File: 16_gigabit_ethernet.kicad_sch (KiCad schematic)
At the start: 29 parts, among them J500 JXD1-1022NL recessed 1GbE RJ45, U500 RTL8111H-CG-RH PCIe Gigabit E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, U501 D3V3XA4B10LP-7 four-channel 0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, U502 D3V3XA4B10LP-7 four-channel 0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, Y500 ECS-250-8-33-AGN-TR 25MHz 8pF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

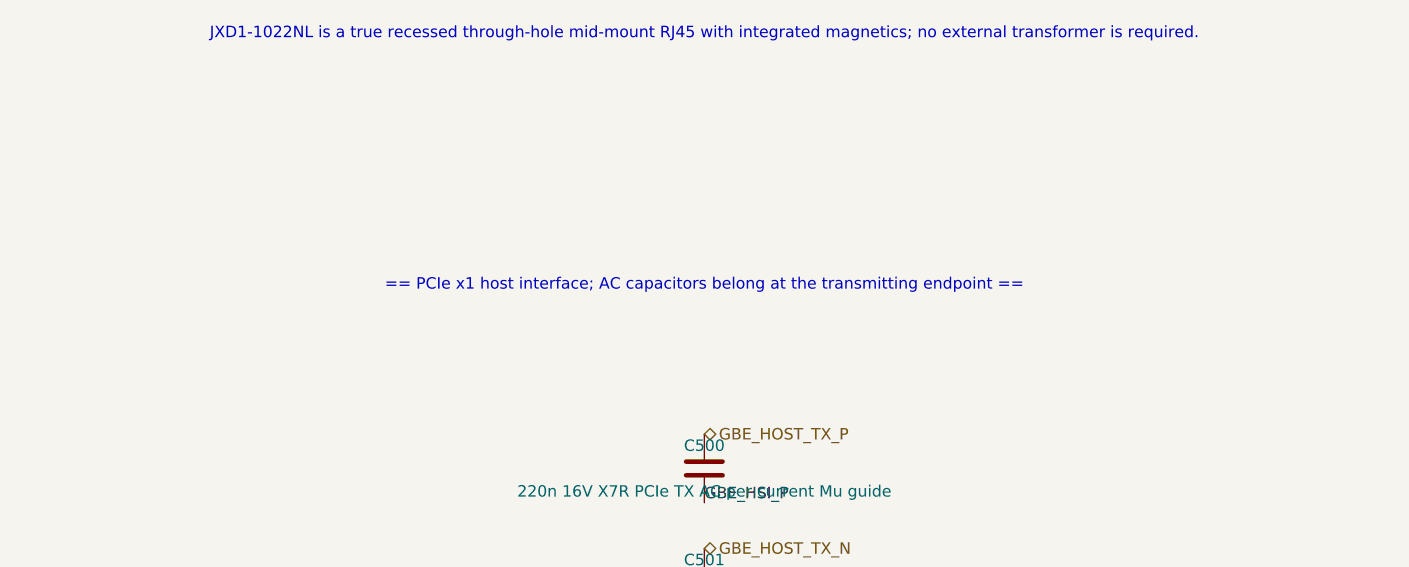
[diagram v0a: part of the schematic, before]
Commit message: Refresh repository with updated PCB renders and current design state
- New 3D renders: top, bottom, perspective, and keyboard PCB
  (generated via kicad-cli 10.0.4, 2560x1440, high quality)
- Update README status: placement complete, coupling caps relocated,
  independent design review CONDITIONAL PASS (2026-07-21)
- Add keyboard rev-A fullboard stencil generation (3MF, STL, manifest, script)
- Track TPS3897ADRYR library symbol
- WIP schematic, PCB, and generator refinements post-coupling-cap fix
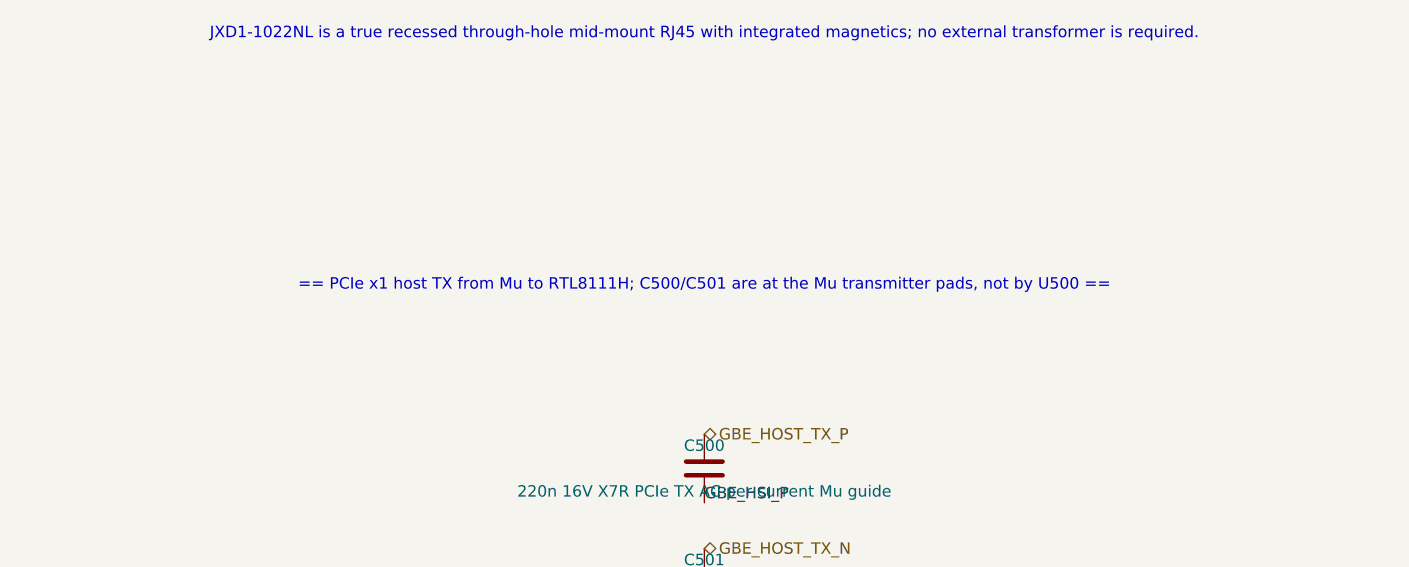
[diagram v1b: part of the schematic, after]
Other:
- note added: "== PCIe x1 host TX from Mu to RTL8111H; C500/C501 are at the Mu transmitter pads, not by U500 =="
- note removed: "== PCIe x1 host interface; AC capacitors belong at the transmitting endpoint =="
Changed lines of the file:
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@@
   (effects (font (size 1.27 1.27)) (justify left bottom))
 )
-(text "== PCIe x1 host interface; AC capacitors belong at the transmitting endpoint ==" (at 20.32 55.88 0) (effects (font (size 1.27 1.27))))
+(text "== PCIe x1 host TX from Mu to RTL8111H; C500/C501 are at the Mu transmitter pads, not by U500 ==" (at 20.32 55.88 0) (effects (font (size 1.27 1.27))))
 (symbol
   (lib_id "Device:C")

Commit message: Assign 327 BOM MPNs across 11 schematic sheets (370→43 gaps)
Closes 370 BOM procurement gaps by assigning Yageo resistor and Murata
capacitor MPNs to all passive components in the project's 11 schematic
sheets. 43 intentional holds remain for design-review items (crystal
loads, audio AC-coupling, VCAP, C0G timing, maker MCU 4.7u 0402s).

Key changes:
- 205 resistors assigned (Yageo RC0603/RT0603 series)
- 124 capacitors assigned (Murata GRM series, matching footprint body size)
- Fixed C183: 4.7u MPN→1u (GRM21BR71A105KA01L)
- Fixed C795/C840: upgraded to 50V rating (GRM21BR71H105KA12L)
- Generated fresh inventory: 1173 components, 43 remaining gaps
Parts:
- C504, C505, C506, C507, C508, C509, C510, C511, C513: MPN (none) -> GRM155R71C104KA88D; Manufacturer (none) -> Murata
- C512: MPN (none) -> GRM31CR71E106KA12L; Manufacturer (none) -> Murata
- R500: MPN (none) -> RC0402FR-071ML; Manufacturer (none) -> Yageo
- R502, R503: MPN (none) -> RC0402FR-0710KL; Manufacturer (none) -> Yageo
- R504, R505: MPN (none) -> RC0402FR-07470RL; Manufacturer (none) -> Yageo
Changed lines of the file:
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@@
   (property "Footprint" "Capacitor_SMD:C_0402_1005Metric" (at 20.32 137.16 0) (effects (font (size 1.27 1.27)) (hide yes)))
   (property "Datasheet" "" (at 20.32 137.16 0) (effects (font (size 1.27 1.27)) (hide yes)))
+  (property "Manufacturer" "Murata" (at 20.32 137.16 0) (effects (font (size 1.27 1.27)) (hide yes)))
+  (property "MPN" "GRM155R71C104KA88D" (at 20.32 137.16 0) (effects (font (size 1.27 1.27)) (hide yes)))
   (pin "1")
   (pin "2")
@@
   (property "Footprint" "Capacitor_SMD:C_0402_1005Metric" (at 20.32 149.86 0) (effects (font (size 1.27 1.27)) (hide yes)))
   (property "Datasheet" "" (at 20.32 149.86 0) (effects (font (size 1.27 1.27)) (hide yes)))
+  (property "Manufacturer" "Murata" (at 20.32 149.86 0) (effects (font (size 1.27 1.27)) (hide yes)))
+  (property "MPN" "GRM155R71C104KA88D" (at 20.32 149.86 0) (effects (font (size 1.27 1.27)) (hide yes)))
   (pin "1")
   (pin "2")
@@
   (property "Footprint" "Capacitor_SMD:C_0402_1005Metric" (at 20.32 162.56 0) (effects (font (size 1.27 1.27)) (hide yes)))
   (property "Datasheet" "" (at 20.32 162.56 0) (effects (font (size 1.27 1.27)) (hide yes)))
+  (property "Manufacturer" "Murata" (at 20.32 162.56 0) (effects (font (size 1.27 1.27)) (hide yes)))
+  (property "MPN" "GRM155R71C104KA88D" (at 20.32 162.56 0) (effects (font (size 1.27 1.27)) (hide yes)))
   (pin "1")
   (pin "2")
@@
   (property "Footprint" "Capacitor_SMD:C_0402_1005Metric" (at 129.54 137.16 0) (effects (font (size 1.27 1.27)) (hide yes)))
   (property "Datasheet" "" (at 129.54 137.16 0) (effects (font (size 1.27 1.27)) (hide yes)))
+  (property "Manufacturer" "Murata" (at 129.54 137.16 0) (effects (font (size 1.27 1.27)) (hide yes)))
+  (property "MPN" "GRM155R71C104KA88D" (at 129.54 137.16 0) (effects (font (size 1.27 1.27)) (hide yes)))
   (pin "1")
   (pin "2")
@@
   (property "Footprint" "Capacitor_SMD:C_0402_1005Metric" (at 129.54 149.86 0) (effects (font (size 1.27 1.27)) (hide yes)))
   (property "Datasheet" "" (at 129.54 149.86 0) (effects (font (size 1.27 1.27)) (hide yes)))
+  (property "Manufacturer" "Murata" (at 129.54 149.86 0) (effects (font (size 1.27 1.27)) (hide yes)))
+  (property "MPN" "GRM155R71C104KA88D" (at 129.54 149.86 0) (effects (font (size 1.27 1.27)) (hide yes)))
   (pin "1")
   (pin "2")
@@
   (property "Footprint" "Capacitor_SMD:C_0402_1005Metric" (at 129.54 162.56 0) (effects (font (size 1.27 1.27)) (hide yes)))
   (property "Datasheet" "" (at 129.54 162.56 0) (effects (font (size 1.27 1.27)) (hide yes)))
+  (property "Manufacturer" "Murata" (at 129.54 162.56 0) (effects (font (size 1.27 1.27)) (hide yes)))
+  (property "MPN" "GRM155R71C104KA88D" (at 129.54 162.56 0) (effects (font (size 1.27 1.27)) (hide yes)))
   (pin "1")
   (pin "2")
@@
   (property "Footprint" "Capacitor_SMD:C_0402_1005Metric" (at 129.54 175.26 0) (effects (font (size 1.27 1.27)) (hide yes)))
   (property "Datasheet" "" (at 129.54 175.26 0) (effects (font (size 1.27 1.27)) (hide yes)))
+  (property "Manufacturer" "Murata" (at 129.54 175.26 0) (effects (font (size 1.27 1.27)) (hide yes)))
+  (property "MPN" "GRM155R71C104KA88D" (at 129.54 175.26 0) (effects (font (size 1.27 1.27)) (hide yes)))
   (pin "1")
   (pin "2")
@@
   (property "Footprint" "Capacitor_SMD:C_0402_1005Metric" (at 129.54 187.96 0) (effects (font (size 1.27 1.27)) (hide yes)))
   (property "Datasheet" "" (at 129.54 187.96 0) (effects (font (size 1.27 1.27)) (hide yes)))
+  (property "Manufacturer" "Murata" (at 129.54 187.96 0) (effects (font (size 1.27 1.27)) (hide yes)))
+  (property "MPN" "GRM155R71C104KA88D" (at 129.54 187.96 0) (effects (font (size 1.27 1.27)) (hide yes)))
   (pin "1")
   (pin "2")
@@
   (property "Footprint" "Capacitor_SMD:C_1206_3216Metric" (at 129.54 200.66 0) (effects (font (size 1.27 1.27)) (hide yes)))
   (property "Datasheet" "" (at 129.54 200.66 0) (effects (font (size 1.27 1.27)) (hide yes)))
+  (property "Manufacturer" "Murata" (at 129.54 200.66 0) (effects (font (size 1.27 1.27)) (hide yes)))
+  (property "MPN" "GRM31CR71E106KA12L" (at 129.54 200.66 0) (effects (font (size 1.27 1.27)) (hide yes)))
   (pin "1")
   (pin "2")
@@
   (property "Footprint" "Resistor_SMD:R_0402_1005Metric" (at 20.32 200.66 0) (effects (font (size 1.27 1.27)) (hide yes)))
   (property "Datasheet" "" (at 20.32 200.66 0) (effects (font (size 1.27 1.27)) (hide yes)))
+  (property "Manufacturer" "Yageo" (at 20.32 200.66 0) (effects (font (size 1.27 1.27)) (hide yes)))
+  (property "MPN" "RC0402FR-0710KL" (at 20.32 200.66 0) (effects (font (size 1.27 1.27)) (hide yes)))
   (pin "1")
   (pin "2")
@@
   (property "Footprint" "Resistor_SMD:R_0402_1005Metric" (at 20.32 213.36 0) (effects (font (size 1.27 1.27)) (hide yes)))
   (property "Datasheet" "" (at 20.32 213.36 0) (effects (font (size 1.27 1.27)) (hide yes)))
+  (property "Manufacturer" "Yageo" (at 20.32 213.36 0) (effects (font (size 1.27 1.27)) (hide yes)))
+  (property "MPN" "RC0402FR-0710KL" (at 20.32 213.36 0) (effects (font (size 1.27 1.27)) (hide yes)))
   (pin "1")
   (pin "2")
@@
   (property "Footprint" "Resistor_SMD:R_0402_1005Metric" (at 149.86 271.78 0) (effects (font (size 1.27 1.27)) (hide yes)))
   (property "Datasheet" "" (at 149.86 271.78 0) (effects (font (size 1.27 1.27)) (hide yes)))
+  (property "Manufacturer" "Yageo" (at 149.86 271.78 0) (effects (font (size 1.27 1.27)) (hide yes)))
+  (property "MPN" "RC0402FR-071ML" (at 149.86 271.78 0) (effects (font (size 1.27 1.27)) (hide yes)))
   (pin "1")
   (pin "2")
@@
   (property "Footprint" "Capacitor_SMD:C_0402_1005Metric" (at 519.43 243.84 0) (effects (font (size 1.27 1.27)) (hide yes)))
   (property "Datasheet" "" (at 519.43 243.84 0) (effects (font (size 1.27 1.27)) (hide yes)))
+  (property "Manufacturer" "Murata" (at 519.43 243.84 0) (effects (font (size 1.27 1.27)) (hide yes)))
+  (property "MPN" "GRM155R71C104KA88D" (at 519.43 243.84 0) (effects (font (size 1.27 1.27)) (hide yes)))
   (pin "1")
   (pin "2")
@@
   (property "Footprint" "Resistor_SMD:R_0402_1005Metric" (at 570.23 256.54 0) (effects (font (size 1.27 1.27)) (hide yes)))
   (property "Datasheet" "" (at 570.23 256.54 0) (effects (font (size 1.27 1.27)) (hide yes)))
+  (property "Manufacturer" "Yageo" (at 570.23 256.54 0) (effects (font (size 1.27 1.27)) (hide yes)))
+  (property "MPN" "RC0402FR-07470RL" (at 570.23 256.54 0) (effects (font (size 1.27 1.27)) (hide yes)))
   (pin "1")
   (pin "2")
@@
   (property "Footprint" "Resistor_SMD:R_0402_1005Metric" (at 570.23 269.24 0) (effects (font (size 1.27 1.27)) (hide yes)))
   (property "Datasheet" "" (at 570.23 269.24 0) (effects (font (size 1.27 1.27)) (hide yes)))
-  (pin "1")
-  (pin "2")
+  (property "Manufacturer" "Yageo" (at 570.23 269.24 0) (effects (font (size 1.27 1.27)) (hide yes)))
+  (property "MPN" "RC0402FR-07470RL" (at 570.23 269.24 0) (effects (font (size 1.27 1.27)) (hide yes)))
+  (pin "1")
+  (pin "2")

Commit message: Regenerate child schematics to sync with current generators
The committed .kicad_sch carried stale embedded Manufacturer/MPN properties from the old per-component BOM approach (MPNs now live in verification/BOM_MPN_ASSIGNMENTS.md). Regenerating from the current generators strips those stale properties and clears the pre-existing Generated-source identity release-check failure. No connectivity change; ERC still 0 errors / 27 intentional warnings; schematic closure 1569/0.
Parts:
- C504, C505, C506, C507, C508, C509, C510, C511, C513: MPN GRM155R71C104KA88D -> (none); Manufacturer Murata -> (none)
- C512: MPN GRM31CR71E106KA12L -> (none); Manufacturer Murata -> (none)
- R500: MPN RC0402FR-071ML -> (none); Manufacturer Yageo -> (none)
- R502, R503: MPN RC0402FR-0710KL -> (none); Manufacturer Yageo -> (none)
- R504, R505: MPN RC0402FR-07470RL -> (none); Manufacturer Yageo -> (none)
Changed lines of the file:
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@@
   (property "Footprint" "Capacitor_SMD:C_0402_1005Metric" (at 20.32 137.16 0) (effects (font (size 1.27 1.27)) (hide yes)))
   (property "Datasheet" "" (at 20.32 137.16 0) (effects (font (size 1.27 1.27)) (hide yes)))
-  (property "Manufacturer" "Murata" (at 20.32 137.16 0) (effects (font (size 1.27 1.27)) (hide yes)))
-  (property "MPN" "GRM155R71C104KA88D" (at 20.32 137.16 0) (effects (font (size 1.27 1.27)) (hide yes)))
   (pin "1")
   (pin "2")
@@
   (property "Footprint" "Capacitor_SMD:C_0402_1005Metric" (at 20.32 149.86 0) (effects (font (size 1.27 1.27)) (hide yes)))
   (property "Datasheet" "" (at 20.32 149.86 0) (effects (font (size 1.27 1.27)) (hide yes)))
-  (property "Manufacturer" "Murata" (at 20.32 149.86 0) (effects (font (size 1.27 1.27)) (hide yes)))
-  (property "MPN" "GRM155R71C104KA88D" (at 20.32 149.86 0) (effects (font (size 1.27 1.27)) (hide yes)))
   (pin "1")
   (pin "2")
@@
   (property "Footprint" "Capacitor_SMD:C_0402_1005Metric" (at 20.32 162.56 0) (effects (font (size 1.27 1.27)) (hide yes)))
   (property "Datasheet" "" (at 20.32 162.56 0) (effects (font (size 1.27 1.27)) (hide yes)))
-  (property "Manufacturer" "Murata" (at 20.32 162.56 0) (effects (font (size 1.27 1.27)) (hide yes)))
-  (property "MPN" "GRM155R71C104KA88D" (at 20.32 162.56 0) (effects (font (size 1.27 1.27)) (hide yes)))
   (pin "1")
   (pin "2")
@@
   (property "Footprint" "Capacitor_SMD:C_0402_1005Metric" (at 129.54 137.16 0) (effects (font (size 1.27 1.27)) (hide yes)))
   (property "Datasheet" "" (at 129.54 137.16 0) (effects (font (size 1.27 1.27)) (hide yes)))
-  (property "Manufacturer" "Murata" (at 129.54 137.16 0) (effects (font (size 1.27 1.27)) (hide yes)))
-  (property "MPN" "GRM155R71C104KA88D" (at 129.54 137.16 0) (effects (font (size 1.27 1.27)) (hide yes)))
   (pin "1")
   (pin "2")
@@
   (property "Footprint" "Capacitor_SMD:C_0402_1005Metric" (at 129.54 149.86 0) (effects (font (size 1.27 1.27)) (hide yes)))
   (property "Datasheet" "" (at 129.54 149.86 0) (effects (font (size 1.27 1.27)) (hide yes)))
-  (property "Manufacturer" "Murata" (at 129.54 149.86 0) (effects (font (size 1.27 1.27)) (hide yes)))
-  (property "MPN" "GRM155R71C104KA88D" (at 129.54 149.86 0) (effects (font (size 1.27 1.27)) (hide yes)))
   (pin "1")
   (pin "2")
@@
   (property "Footprint" "Capacitor_SMD:C_0402_1005Metric" (at 129.54 162.56 0) (effects (font (size 1.27 1.27)) (hide yes)))
   (property "Datasheet" "" (at 129.54 162.56 0) (effects (font (size 1.27 1.27)) (hide yes)))
-  (property "Manufacturer" "Murata" (at 129.54 162.56 0) (effects (font (size 1.27 1.27)) (hide yes)))
-  (property "MPN" "GRM155R71C104KA88D" (at 129.54 162.56 0) (effects (font (size 1.27 1.27)) (hide yes)))
   (pin "1")
   (pin "2")
@@
   (property "Footprint" "Capacitor_SMD:C_0402_1005Metric" (at 129.54 175.26 0) (effects (font (size 1.27 1.27)) (hide yes)))
   (property "Datasheet" "" (at 129.54 175.26 0) (effects (font (size 1.27 1.27)) (hide yes)))
-  (property "Manufacturer" "Murata" (at 129.54 175.26 0) (effects (font (size 1.27 1.27)) (hide yes)))
-  (property "MPN" "GRM155R71C104KA88D" (at 129.54 175.26 0) (effects (font (size 1.27 1.27)) (hide yes)))
   (pin "1")
   (pin "2")
@@
   (property "Footprint" "Capacitor_SMD:C_0402_1005Metric" (at 129.54 187.96 0) (effects (font (size 1.27 1.27)) (hide yes)))
   (property "Datasheet" "" (at 129.54 187.96 0) (effects (font (size 1.27 1.27)) (hide yes)))
-  (property "Manufacturer" "Murata" (at 129.54 187.96 0) (effects (font (size 1.27 1.27)) (hide yes)))
-  (property "MPN" "GRM155R71C104KA88D" (at 129.54 187.96 0) (effects (font (size 1.27 1.27)) (hide yes)))
   (pin "1")
   (pin "2")
@@
   (property "Footprint" "Capacitor_SMD:C_1206_3216Metric" (at 129.54 200.66 0) (effects (font (size 1.27 1.27)) (hide yes)))
   (property "Datasheet" "" (at 129.54 200.66 0) (effects (font (size 1.27 1.27)) (hide yes)))
-  (property "Manufacturer" "Murata" (at 129.54 200.66 0) (effects (font (size 1.27 1.27)) (hide yes)))
-  (property "MPN" "GRM31CR71E106KA12L" (at 129.54 200.66 0) (effects (font (size 1.27 1.27)) (hide yes)))
   (pin "1")
   (pin "2")
@@
   (property "Footprint" "Resistor_SMD:R_0402_1005Metric" (at 20.32 200.66 0) (effects (font (size 1.27 1.27)) (hide yes)))
   (property "Datasheet" "" (at 20.32 200.66 0) (effects (font (size 1.27 1.27)) (hide yes)))
-  (property "Manufacturer" "Yageo" (at 20.32 200.66 0) (effects (font (size 1.27 1.27)) (hide yes)))
-  (property "MPN" "RC0402FR-0710KL" (at 20.32 200.66 0) (effects (font (size 1.27 1.27)) (hide yes)))
   (pin "1")
   (pin "2")
@@
   (property "Footprint" "Resistor_SMD:R_0402_1005Metric" (at 20.32 213.36 0) (effects (font (size 1.27 1.27)) (hide yes)))
   (property "Datasheet" "" (at 20.32 213.36 0) (effects (font (size 1.27 1.27)) (hide yes)))
-  (property "Manufacturer" "Yageo" (at 20.32 213.36 0) (effects (font (size 1.27 1.27)) (hide yes)))
-  (property "MPN" "RC0402FR-0710KL" (at 20.32 213.36 0) (effects (font (size 1.27 1.27)) (hide yes)))
   (pin "1")
   (pin "2")
@@
   (property "Footprint" "Resistor_SMD:R_0402_1005Metric" (at 149.86 271.78 0) (effects (font (size 1.27 1.27)) (hide yes)))
   (property "Datasheet" "" (at 149.86 271.78 0) (effects (font (size 1.27 1.27)) (hide yes)))
-  (property "Manufacturer" "Yageo" (at 149.86 271.78 0) (effects (font (size 1.27 1.27)) (hide yes)))
-  (property "MPN" "RC0402FR-071ML" (at 149.86 271.78 0) (effects (font (size 1.27 1.27)) (hide yes)))
   (pin "1")
   (pin "2")
@@
   (property "Footprint" "Capacitor_SMD:C_0402_1005Metric" (at 519.43 243.84 0) (effects (font (size 1.27 1.27)) (hide yes)))
   (property "Datasheet" "" (at 519.43 243.84 0) (effects (font (size 1.27 1.27)) (hide yes)))
-  (property "Manufacturer" "Murata" (at 519.43 243.84 0) (effects (font (size 1.27 1.27)) (hide yes)))
-  (property "MPN" "GRM155R71C104KA88D" (at 519.43 243.84 0) (effects (font (size 1.27 1.27)) (hide yes)))
   (pin "1")
   (pin "2")
@@
   (property "Footprint" "Resistor_SMD:R_0402_1005Metric" (at 570.23 256.54 0) (effects (font (size 1.27 1.27)) (hide yes)))
   (property "Datasheet" "" (at 570.23 256.54 0) (effects (font (size 1.27 1.27)) (hide yes)))
-  (property "Manufacturer" "Yageo" (at 570.23 256.54 0) (effects (font (size 1.27 1.27)) (hide yes)))
-  (property "MPN" "RC0402FR-07470RL" (at 570.23 256.54 0) (effects (font (size 1.27 1.27)) (hide yes)))
   (pin "1")
   (pin "2")
@@
   (property "Footprint" "Resistor_SMD:R_0402_1005Metric" (at 570.23 269.24 0) (effects (font (size 1.27 1.27)) (hide yes)))
   (property "Datasheet" "" (at 570.23 269.24 0) (effects (font (size 1.27 1.27)) (hide yes)))
-  (property "Manufacturer" "Yageo" (at 570.23 269.24 0) (effects (font (size 1.27 1.27)) (hide yes)))
-  (property "MPN" "RC0402FR-07470RL" (at 570.23 269.24 0) (effects (font (size 1.27 1.27)) (hide yes)))
-  (pin "1")
-  (pin "2")
+  (pin "1")
+  (pin "2")
